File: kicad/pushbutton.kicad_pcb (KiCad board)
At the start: 2 copper layers, 86.4 x 41.9 mm, 19 parts, among them J1 USB_B_Micro, J2 Conn_01x02_Male, Q1 SI2301, Q2 IRLML6402, Q3 S8050_J3Y, Q4 S8050_J3Y, Q5 PUMX1, Q6 PMBT2222AYS, SW1 SW_Push, U1 MAX16054, U2 MCP73831-2-OT, U3 TLV75533PDBV, U4 CP2102-GMR_NRND, U5 ESP-12F

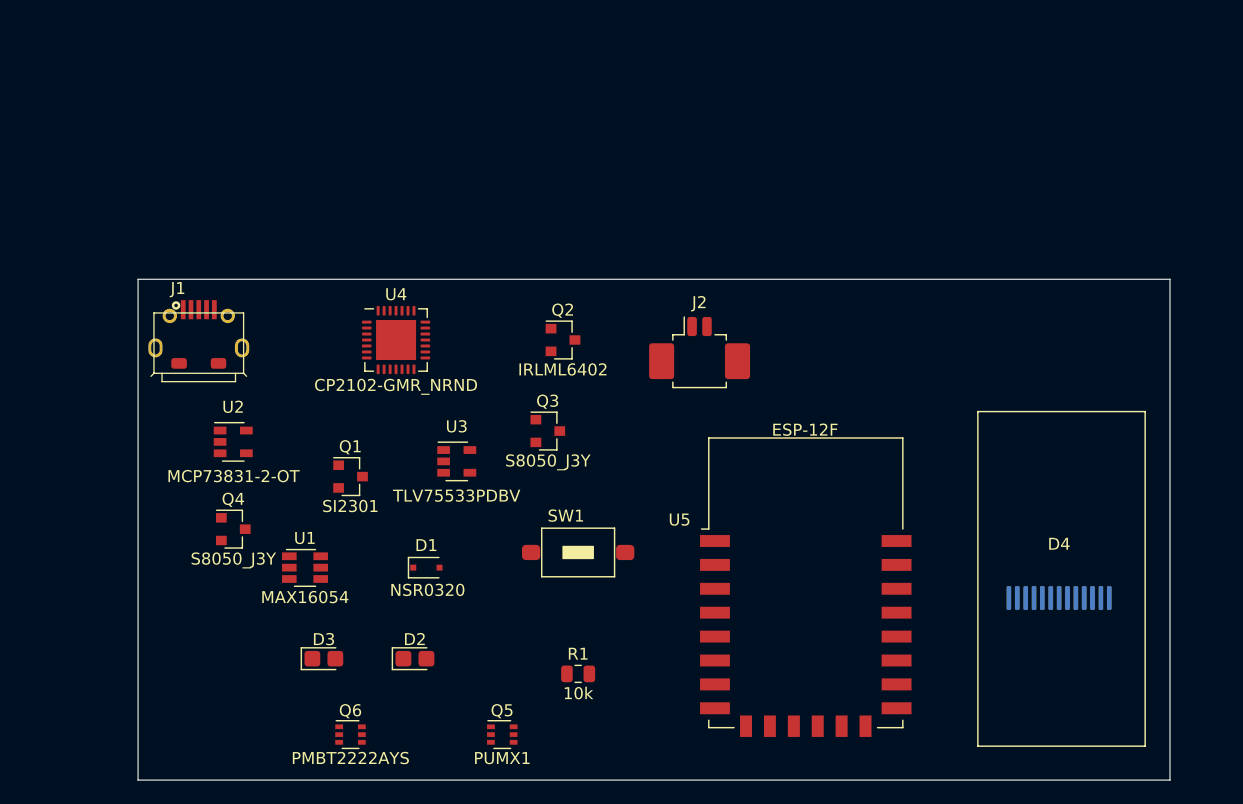
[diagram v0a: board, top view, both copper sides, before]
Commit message: Extended schematics
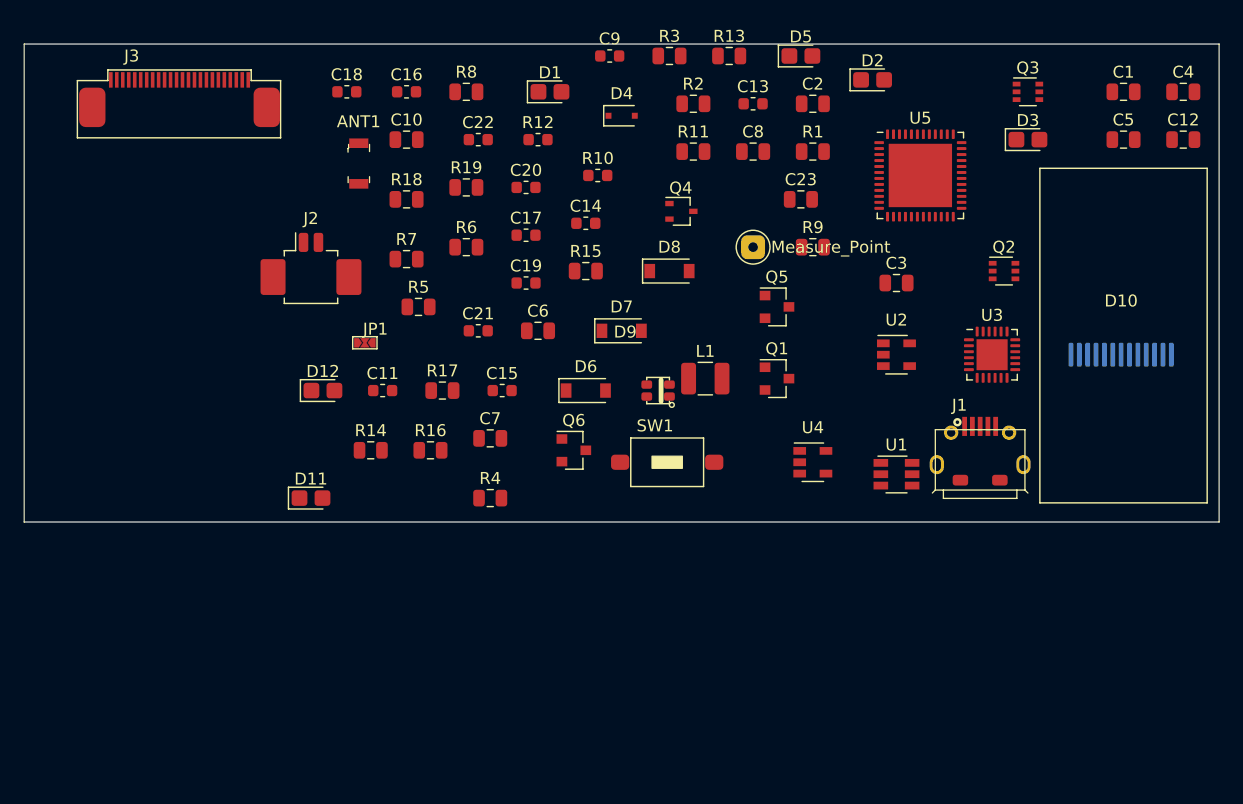
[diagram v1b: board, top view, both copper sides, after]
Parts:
- added ANT1: 2450AT18A100E, digikey-footprints:Antenna_1.6x3.2mm_2450AT18A100E, F.Cu at (68.0, 50.0)
- added C1: 100n, Capacitor_SMD:C_0805_2012Metric, F.Cu at (132.0, 44.0)
- added C10: 1u, Capacitor_SMD:C_0805_2012Metric, F.Cu at (72.0, 48.0)
- added C11: 100n, Capacitor_SMD:C_0603_1608Metric, F.Cu at (70.0, 69.0)
- added C12: 100n, Capacitor_SMD:C_0805_2012Metric, F.Cu at (137.0, 48.0)
- added C13: 100n, Capacitor_SMD:C_0603_1608Metric, F.Cu at (101.0, 45.0)
- added C14: 1u, Capacitor_SMD:C_0603_1608Metric, F.Cu at (87.0, 55.0)
- added C15: 1u, Capacitor_SMD:C_0603_1608Metric, F.Cu at (80.0, 69.0)
- added C16: 1u, Capacitor_SMD:C_0603_1608Metric, F.Cu at (72.0, 44.0)
- added C17: 1u, Capacitor_SMD:C_0603_1608Metric, F.Cu at (82.0, 56.0)
- added C18: 1u, Capacitor_SMD:C_0603_1608Metric, F.Cu at (67.0, 44.0)
- added C19: 1u, Capacitor_SMD:C_0603_1608Metric, F.Cu at (82.0, 60.0)
- added C2: 1u, Capacitor_SMD:C_0805_2012Metric, F.Cu at (106.0, 45.0)
- added C20: 1u, Capacitor_SMD:C_0603_1608Metric, F.Cu at (82.0, 52.0)
- added C21: 1u, Capacitor_SMD:C_0603_1608Metric, F.Cu at (78.0, 64.0)
- added C22: 1u, Capacitor_SMD:C_0603_1608Metric, F.Cu at (78.0, 48.0)
- added C23: 100n, Capacitor_SMD:C_0805_2012Metric, F.Cu at (105.0, 53.0)
- added C3: 4.7u, Capacitor_SMD:C_0805_2012Metric, F.Cu at (113.0, 60.0)
- added C4: 4.7u, Capacitor_SMD:C_0805_2012Metric, F.Cu at (137.0, 44.0)
- added C5: 4.7u, Capacitor_SMD:C_0805_2012Metric, F.Cu at (132.0, 48.0)
- added C6: 1u, Capacitor_SMD:C_0805_2012Metric, F.Cu at (83.0, 64.0)
- added C7: 4.7u, Capacitor_SMD:C_0805_2012Metric, F.Cu at (79.0, 73.0)
- added C8: 1u, Capacitor_SMD:C_0805_2012Metric, F.Cu at (101.0, 49.0)
- added C9: 4.7u, Capacitor_SMD:C_0603_1608Metric, F.Cu at (89.0, 41.0)
- added D10: IPSDisplay_80x160, barn53-kicad:IPS_Display_80x160_Bottom_1.6mm, F.Cu at (136.0, 66.0)
- added D11: LED Red, LED_SMD:LED_0805_2012Metric_Castellated, F.Cu at (64.0, 78.0)
- added D12: LED Blue, LED_SMD:LED_0805_2012Metric_Castellated, F.Cu at (65.0, 69.0)
- added D5: RxD, LED_SMD:LED_0805_2012Metric_Castellated, F.Cu at (105.0, 41.0)
- added D6: MBR0530, Diode_SMD:D_SOD-123, F.Cu at (87.0, 69.0)
- added D7: MBR0530, Diode_SMD:D_SOD-123, F.Cu at (90.0, 64.0)
- added D8: MBR0530, Diode_SMD:D_SOD-123, F.Cu at (94.0, 59.0)
- added D9: WS2812B-2020, barn53-kicad:WS2812B-2020, F.Cu at (93.0, 69.0)
- added J3: Conn_01x24, barn53-kicad:FPC_24_JUSHUO-AFC07-S24ECA, F.Cu at (53.0, 43.0)
- added JP1: SolderJumper_3_Open, barn53-kicad:SolderJumper-3_small, F.Cu at (68.0, 65.0)
- added L1: 68uH, Inductor_SMD:L_1210_3225Metric, F.Cu at (97.0, 68.0)
- added M1: Measure_Point, barn53-kicad:Measure_Point_Through, F.Cu at (101.0, 57.0)
- added R10: 10k, Resistor_SMD:R_0603_1608Metric, F.Cu at (88.0, 51.0)
- added R11: 10k, Resistor_SMD:R_0805_2012Metric, F.Cu at (96.0, 49.0)
- added R12: 0.47, Resistor_SMD:R_0603_1608Metric, F.Cu at (83.0, 48.0)
- added R13: 10k, Resistor_SMD:R_0805_2012Metric, F.Cu at (99.0, 41.0)
- added R14: 1k, Resistor_SMD:R_0805_2012Metric, F.Cu at (69.0, 74.0)
- added R15: 10k, Resistor_SMD:R_0805_2012Metric, F.Cu at (87.0, 59.0)
- added R16: 10k, Resistor_SMD:R_0805_2012Metric, F.Cu at (74.0, 74.0)
- added R17: 10, Resistor_SMD:R_0805_2012Metric, F.Cu at (75.0, 69.0)
- added R18: ?, Resistor_SMD:R_0805_2012Metric, F.Cu at (72.0, 53.0)
- added R19: ?, Resistor_SMD:R_0805_2012Metric, F.Cu at (77.0, 52.0)
- added R2: 470, Resistor_SMD:R_0805_2012Metric, F.Cu at (96.0, 45.0)
- added R3: 470, Resistor_SMD:R_0805_2012Metric, F.Cu at (94.0, 41.0)
- added R4: 10k, Resistor_SMD:R_0805_2012Metric, F.Cu at (79.0, 78.0)
- added R5: 180, Resistor_SMD:R_0805_2012Metric, F.Cu at (73.0, 62.0)
- added R6: 180, Resistor_SMD:R_0805_2012Metric, F.Cu at (77.0, 57.0)
- added R7: 10k, Resistor_SMD:R_0805_2012Metric, F.Cu at (72.0, 58.0)
- added R8: 10k, Resistor_SMD:R_0805_2012Metric, F.Cu at (77.0, 44.0)
- added R9: 100k, Resistor_SMD:R_0805_2012Metric, F.Cu at (106.0, 57.0)
- D1: value NSR0320 -> charge; footprint Diode_SMD:D_SOD-323F -> LED_SMD:LED_0805_2012Metric_Castellated
- D2: value LED Blue -> ready
- D3: value LED Red -> TxD
- D4: value IPSDisplay_80x160 -> NSR0320; footprint barn53-kicad:IPS_Display_80x160_Bottom_1.6mm -> Diode_SMD:D_SOD-323F
- Q2: value IRLML6402 -> PMBT2222AYS; footprint Package_TO_SOT_SMD:SOT-23 -> Package_TO_SOT_SMD:SOT-363_SC-70-6
- Q3: value S8050_J3Y -> PMBT2222AYS; footprint Package_TO_SOT_SMD:SOT-23 -> Package_TO_SOT_SMD:SOT-363_SC-70-6
- Q4: value S8050_J3Y -> Si1308EDL; footprint Package_TO_SOT_SMD:SOT-23 -> Package_TO_SOT_SMD:SOT-323_SC-70
- Q5: value PUMX1 -> IRLML6402; footprint Package_TO_SOT_SMD:SOT-363_SC-70-6 -> Package_TO_SOT_SMD:SOT-23
- Q6: value PMBT2222AYS -> S8050_J3Y; footprint Package_TO_SOT_SMD:SOT-363_SC-70-6 -> Package_TO_SOT_SMD:SOT-23
- R1: value 10k -> 2k
- U3: value TLV75533PDBV -> CP2104; footprint Package_TO_SOT_SMD:SOT-23-5 -> Package_DFN_QFN:QFN-24-1EP_4x4mm_P0.5mm_EP2.6x2.6mm
- U4: value CP2102-GMR_NRND -> TLV75533PDBV; footprint Package_DFN_QFN:QFN-28-1EP_5x5mm_P0.5mm_EP3.35x3.35mm -> Package_TO_SOT_SMD:SOT-23-5
- U5: value ESP-12F -> ESP32-PICO-D4; footprint barn53-kicad:ESP-12E -> Package_DFN_QFN:QFN-48-1EP_7x7mm_P0.5mm_EP5.3x5.3mm
- moved D3 73.2 mm to (124.0, 48.0)
- moved J1 66.1 mm to (120.0, 72.0)
- moved D2 61.8 mm to (111.0, 43.0)
- moved D4 57.4 mm to (90.0, 46.0)
- moved U2 56.0 mm to (113.0, 66.0)
- moved U1 50.1 mm to (113.0, 76.0)
- moved Q3 49.2 mm to (124.0, 44.0)
- moved R1 47.9 mm to (106.0, 49.0)
- moved Q4 46.0 mm to (95.0, 54.0)
- moved U3 45.7 mm to (121.0, 66.0)
- moved Q5 42.5 mm to (103.0, 62.0)
- moved D1 41.1 mm to (84.0, 44.0)
- moved Q2 37.4 mm to (122.0, 59.0)
- moved Q1 36.6 mm to (103.0, 68.0)
- moved U4 36.3 mm to (106.0, 75.0)
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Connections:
- D1 pad 1: (no net) -> Net-(D1-Pad1)
- D1 pad 2: (no net) -> Net-(D1-Pad2)
- D2 pad 1: (no net) -> Net-(D2-Pad1)
- D2 pad 2: (no net) -> Net-(D1-Pad1)
- D3 pad 1: (no net) -> Net-(D3-Pad1)
- D3 pad 2: (no net) -> /VDD
- D4 pad 1: (no net) -> /VSupp
- D4 pad 2: (no net) -> /VBus
- J1 pad 1: (no net) -> /VBus
- J1 pad 2: (no net) -> /D-
- J1 pad 3: (no net) -> /D+
- J1 pad 5: (no net) -> GND
- J1 pad 6: Net-(J1-Pad6) -> GND
- Q1 pad 1: (no net) -> /VBus
- Q1 pad 2: (no net) -> /VSupp
- Q1 pad 3: (no net) -> /VBat
- Q2 pad 1: (no net) -> /RTS
- Q2 pad 2: (no net) -> Net-(Q2-Pad2)
- Q3 pad 1: (no net) -> /DTR
- Q3 pad 2: (no net) -> Net-(Q3-Pad2)
- Q4 pad 1: (no net) -> /EPD_GDR
- Q4 pad 2: (no net) -> /EPD_RESE
- Q4 pad 3: (no net) -> Net-(C11-Pad1)
- Q5 pad 1: (no net) -> /~Switch
- Q5 pad 2: (no net) -> /VSupp
- Q5 pad 3: (no net) -> /VSwitched
- Q6 pad 1: (no net) -> Net-(Q6-Pad1)
- Q6 pad 2: (no net) -> GND
- Q6 pad 3: (no net) -> Net-(Q6-Pad3)
- R1 pad 1: (no net) -> Net-(R1-Pad1)
- R1 pad 2: (no net) -> GND
- SW1 pad 1: (no net) -> GND
- SW1 pad 2: (no net) -> Net-(SW1-Pad2)
- U1 pad 1: (no net) -> Net-(SW1-Pad2)
- U1 pad 2: (no net) -> GND
- U1 pad 3: (no net) -> GND
- U1 pad 5: (no net) -> /LDO_EN
- U1 pad 6: (no net) -> /VSupp
- U2 pad 1: (no net) -> Net-(D1-Pad1)
- U2 pad 2: (no net) -> GND
- U2 pad 3: (no net) -> /VBat
- U2 pad 4: (no net) -> /VBus
- U2 pad 5: (no net) -> Net-(R1-Pad1)
- U3 pad 2: (no net) -> GND
- U3 pad 3: (no net) -> /D+
- U3 pad 4: (no net) -> /D-
- U3 pad 5: (no net) -> /VDD
- U4 pad 1: (no net) -> /VSupp
- U4 pad 2: (no net) -> GND
- U4 pad 3: (no net) -> /LDO_EN
- U4 pad 5: (no net) -> +3V3
- U5 pad 1: (no net) -> Net-(U5-Pad1)
- U5 pad 3: (no net) -> Net-(U5-Pad3)
- U5 pad 4: (no net) -> Net-(U5-Pad3)
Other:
- board size 86.4 x 41.9 mm -> 100 x 40 mm
